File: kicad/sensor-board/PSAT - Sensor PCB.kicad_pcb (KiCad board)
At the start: 2 copper layers, 54.5 x 54.5 mm, 52 parts, among them J1 533980471, J2 533980471, J3 533980471, J4 533980471, Q1 2N2222A, U1 CD-PA1616D, U2 ESP32-CAM, U4 BMI323

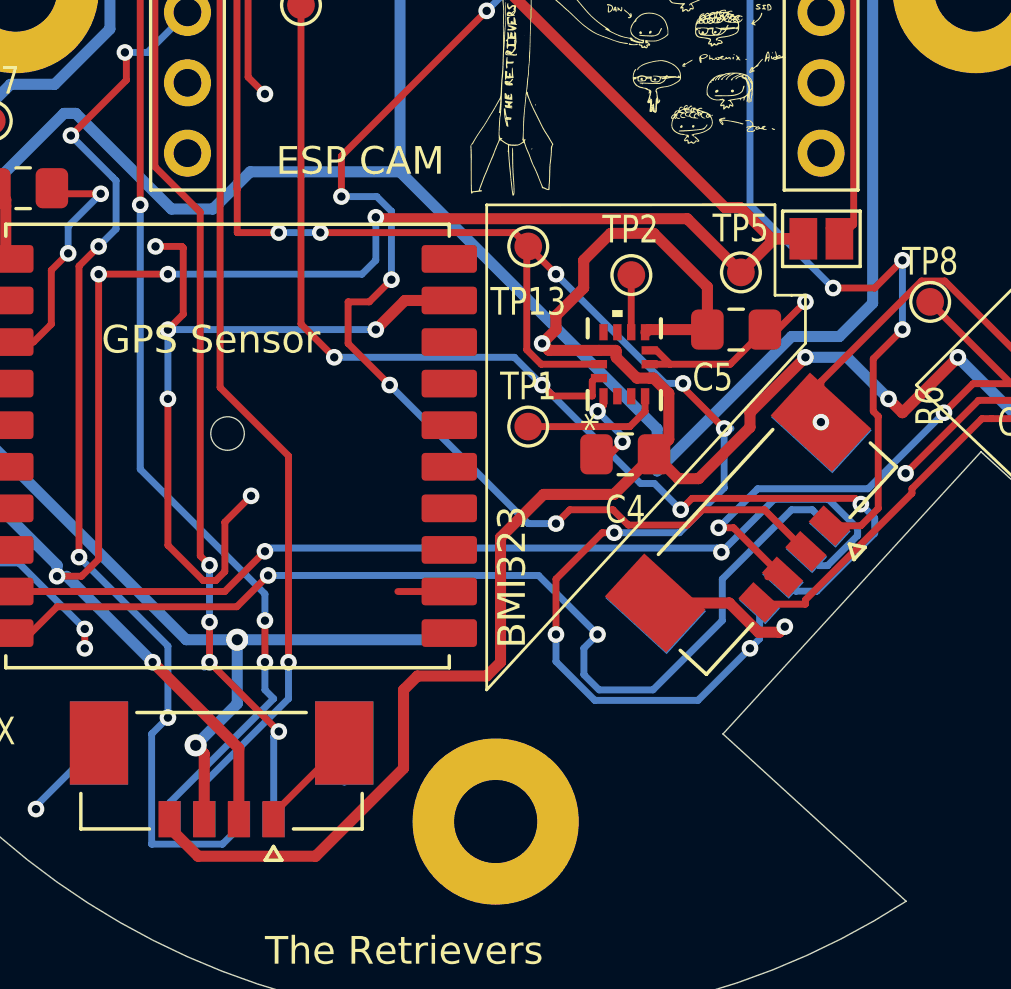
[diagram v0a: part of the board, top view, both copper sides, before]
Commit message: feat: Aidan review this: fixed righted angle wires
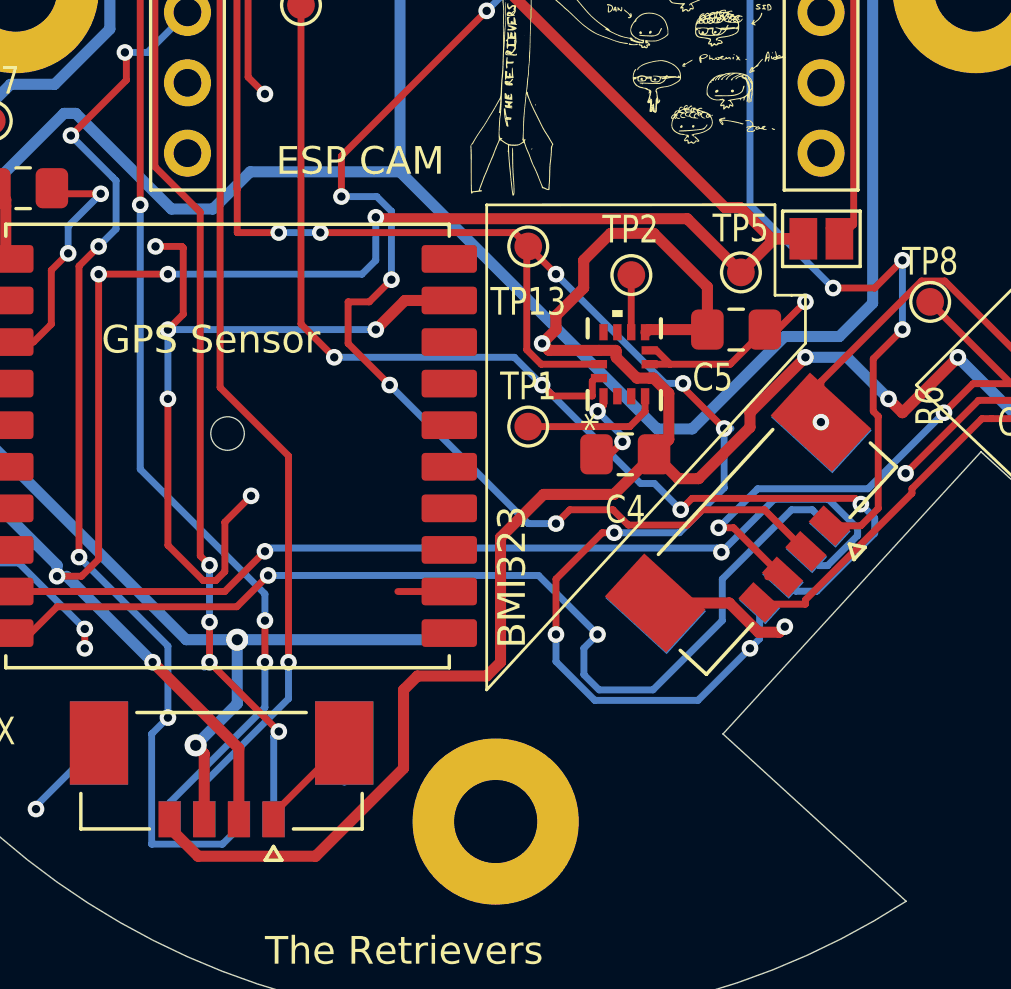
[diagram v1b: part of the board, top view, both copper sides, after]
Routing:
- net 3V3_LDO: track 199.1 -> 196.9 mm
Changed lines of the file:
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@@
-	)
-	(segment
-		(start 153 99.75)
-		(end 154.725 99.75)
-		(width 0.4)
-		(layer "B.Cu")
-		(net 8)
-	)
-	(segment
-		(start 148.15 104.6)
-		(end 148.15 103.083714)
-		(width 0.4)
-		(layer "B.Cu")
-		(net 8)
 	)
 	(segment
@@
 	)
 	(segment
-		(start 148.15 103.083714)
-		(end 138.875 93.808714)
+		(start 130.625 95.15)
+		(end 132.125 95.15)
+		(width 0.4)
+		(layer "B.Cu")
+		(net 8)
+	)
+	(segment
+		(start 121.775 96.675)
+		(end 126.75 91.7)
+		(width 0.4)
+		(layer "B.Cu")
+		(net 8)
+	)
+	(segment
+		(start 127.175 91.7)
+		(end 130.625 95.15)
+		(width 0.4)
+		(layer "B.Cu")
+		(net 8)
+	)
+	(segment
+		(start 138.875 93.808714)
+		(end 148.15 103.083714)
+		(width 0.4)
+		(layer "B.Cu")
+		(net 8)
+	)
+	(segment
+		(start 164.897 106.397)
+		(end 165.8 106.397)
+		(width 0.4)
+		(layer "B.Cu")
+		(net 8)
+	)
+	(segment
+		(start 155.925 85.325)
+		(end 156.5 84.75)
+		(width 0.4)
+		(layer "B.Cu")
+		(net 8)
+	)
+	(segment
+		(start 153.5 100.5)
+		(end 155 100.5)
+		(width 0.4)
+		(layer "B.Cu")
+		(net 8)
+	)
+	(segment
+		(start 119.825 96.675)
+		(end 121.775 96.675)
+		(width 0.4)
+		(layer "B.Cu")
+		(net 8)
+	)
+	(segment
+		(start 155 100.5)
+		(end 156.5 102)
 		(width 0.4)
 		(layer "B.Cu")
@@
 	)
 	(segment
-		(start 130.625 95.15)
-		(end 132.125 95.15)
-		(width 0.4)
-		(layer "B.Cu")
-		(net 8)
-	)
-	(segment
-		(start 121.775 96.675)
-		(end 126.75 91.7)
-		(width 0.4)
-		(layer "B.Cu")
-		(net 8)
-	)
-	(segment
-		(start 127.175 91.7)
-		(end 130.625 95.15)
-		(width 0.4)
-		(layer "B.Cu")
-		(net 8)
-	)
-	(segment
-		(start 148.15 104.6)
-		(end 153 99.75)
-		(width 0.4)
-		(layer "B.Cu")
-		(net 8)
-	)
-	(segment
-		(start 164.897 106.397)
-		(end 165.8 106.397)
-		(width 0.4)
-		(layer "B.Cu")
-		(net 8)
-	)
-	(segment
-		(start 153.5 100.5)
-		(end 155 100.5)
-		(width 0.4)
-		(layer "B.Cu")
-		(net 8)
-	)
-	(segment
-		(start 119.825 96.675)
-		(end 121.775 96.675)
-		(width 0.4)
-		(layer "B.Cu")
-		(net 8)
-	)
-	(segment
-		(start 155 100.5)
-		(end 156.5 102)
-		(width 0.4)
-		(layer "B.Cu")
-		(net 8)
-	)
-	(segment
-		(start 155.925 85.325)
-		(end 156.5 84.75)
-		(width 0.4)
-		(layer "B.Cu")
-		(net 8)
-	)
-	(segment
 		(start 142 84)
 		(end 139.6 84)
@@
 	)
 	(segment
+		(start 149.416286 103.083714)
+		(end 148.15 103.083714)
+		(width 0.4)
+		(layer "B.Cu")
+		(net 8)
+	)
+	(segment
+		(start 152.75 99.75)
+		(end 149.416286 103.083714)
+		(width 0.4)
+		(layer "B.Cu")
+		(net 8)
+	)
+	(segment
 		(start 119 97.5)
 		(end 119.825 96.675)
@@
 	)
 	(segment
+		(start 154.725 99.75)
+		(end 155.925 98.55)
+		(width 0.4)
+		(layer "B.Cu")
+		(net 8)
+	)
+	(segment
 		(start 159 100.5)
 		(end 164.897 106.397)
@@
 	)
 	(segment
-		(start 154.725 99.75)
-		(end 155.925 98.55)
-		(width 0.4)
-		(layer "B.Cu")
-		(net 8)
-	)
-	(segment
 		(start 133.466286 93.808714)
 		(end 138.875 93.808714)
@@
 	)
 	(segment
+		(start 152.75 99.75)
+		(end 154.725 99.75)
+		(width 0.4)
+		(layer "B.Cu")
+		(net 8)
+	)
+	(segment
 		(start 154.364302 106.577027)
 		(end 155.501034 106.577027)
@@
 	)
 	(segment
-		(start 134 111.5)
-		(end 134 112.5)
+		(start 134 113.131694)
+		(end 130.565847 116.565847)
 		(width 0.25)
 		(layer "B.Cu")
@@
 	)
 	(segment
-		(start 130.565847 117.162836)
-		(end 130.565847 116.565847)
-		(width 0.25)
-		(layer "B.Cu")
-		(net 14)
-	)
-	(segment
-		(start 134 112.5)
-		(end 134.315847 112.815847)
-		(width 0.25)
-		(layer "B.Cu")
-		(net 14)
-	)
-	(segment
 		(start 134 109.037939)
 		(end 134 110)
@@
 	)
 	(segment
+		(start 134 111.5)
+		(end 134 113.131694)
+		(width 0.25)
+		(layer "B.Cu")
+		(net 14)
+	)
+	(segment
 		(start 130.565847 116.565847)
-		(end 134.315847 112.815847)
-		(width 0.25)
-		(layer "B.Cu")
+		(end 130.565847 117.162836)
+		(width 0.25)
+		(layer "B.Cu")

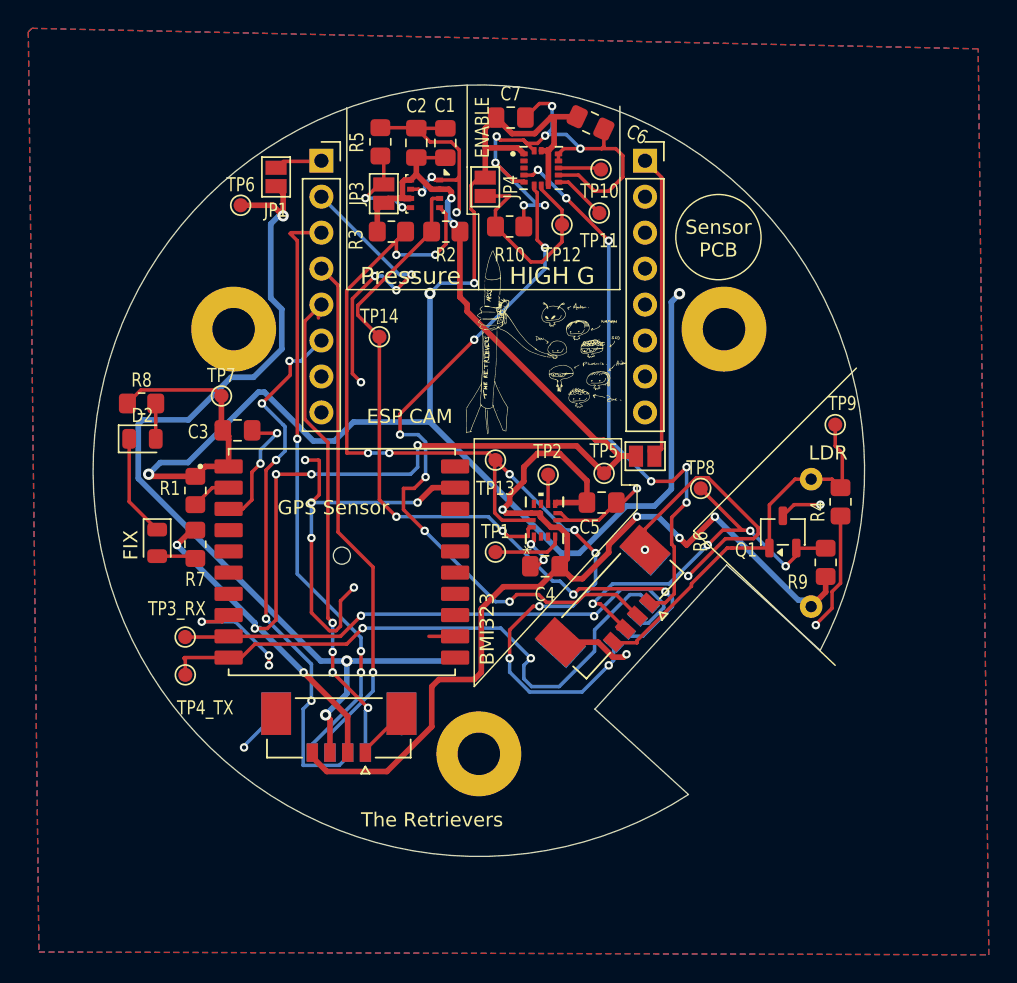
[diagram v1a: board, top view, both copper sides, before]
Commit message: feat: added improvements and removed irrelevant components
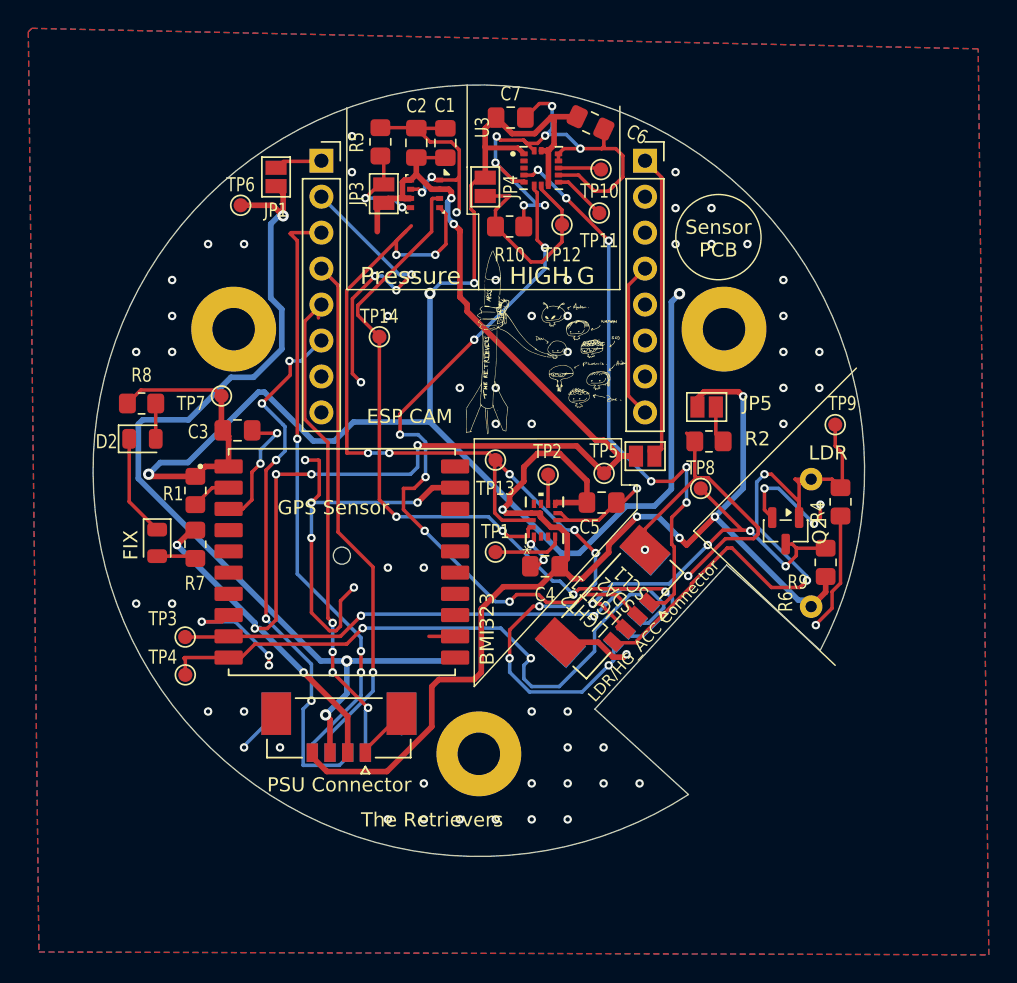
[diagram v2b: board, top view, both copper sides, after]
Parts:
- removed the G*** at (142.1, 84.1)
- removed Q1: 2N2222A, Package_TO_SOT_SMD:SOT-23-3
- removed R3: 4.7k, Resistor_SMD:R_0805_2012Metric_Pad1.20x1.40mm_HandSolder
- added JP5: EN_5, Jumper:SolderJumper-2_P1.3mm_Open_Pad1.0x1.5mm, F.Cu at (158.4, 92.8)
- added Q2: Q_NPN_BEC, Package_TO_SOT_SMD:SOT-23, F.Cu at (164.0, 101.5)
- R2: value 4.7k -> 1Meg
- R7, R8: value 1k -> 5.1k
- R9: value 10k -> 100k
- moved R2 23.8 mm to (158.6, 95.2), turned to 180 degrees
- renumbered TP3_RX to TP3, TP4_TX to TP4, ENABLE to U3, ESP32 to U5
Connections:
- R2 pad 1: SDA1 -> SDO
- R2 pad 2: 3V3_BUCK -> GND
- U2 pad 12: unconnected-(U2-GND.-Pad12) -> GND
- U2 pad 16: unconnected-(U2-.GND-Pad16) -> GND
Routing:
- net GND: track 186.9 -> 207.6 mm, vias 33 -> 88
- net LIGHT2: track 27.8 -> 42.6 mm, vias 0 -> 2
- net 3V3_LDO: track 196.9 -> 210.4 mm, vias 8 -> 9
- net SDO: track 0.00 -> 2.64 mm
- net LIGHT1: track 28.3 -> 29.1 mm
- net unconnected-(U2-.GND-Pad16): track 0.70 -> 0.00 mm
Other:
- board text added: "CAM Connector"
- board text added: "GPS/BOSCH Connector"
- board text added: "LDR/HG_ACC Connector"
- board text added: "LIGHT 1"
- board text added: "LIGHT2"
- board text added: "PSU Connector"
- board text added: "SCL1"
- board text added: "SDA2"
- board text removed: "Never gonna give you up Never gonna let you down Never gonna run around and desert you Never gonna make you cry Never gonna say goodbye Never gonna tell a lie and hurt you"

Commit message: fix: silkscreen labels sensor board
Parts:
- moved 5V 0.50 mm to (125.5, 78.0)
- renumbered TP5 to 3V3B, TP7 to 3V3L, TP6 to 5V, TP10 to I1100, TP1 to I1323, TP11 to I2100, TP2 to I2323, TP8 to L1, TP9 to L2, TP4 to RX, TP12 to SA0, TP13 to SCL1, TP14 to SDA1, TP3 to TX
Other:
- board text removed: "LIGHT 1"
- board text removed: "LIGHT2"
- board text removed: "SCL1"
- board text removed: "SDA2"

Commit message: feat: added image
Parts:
- added G***: LOGO, Image_Converter:BIGGIE, B.Cu at (142.7, 89.5)
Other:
- board text added: "Bombastic, romantic, fantastic, I'm Mr. Boombastic"
- board text added: "NOBI"
